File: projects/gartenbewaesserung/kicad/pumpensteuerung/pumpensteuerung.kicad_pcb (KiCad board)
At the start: 2 copper layers, 100 x 85 mm, 26 parts, among them J1 Screw_Terminal_01x03, J2 Screw_Terminal_01x02, J3 I2C Terminal, J4 Screw_Terminal_01x03, J5 Screw_Terminal_01x03, K2 SANYOU_SRD_Form_C, K3 SANYOU_SRD_Form_C, K4 SANYOU_SRD_Form_C, Q1 S8050, Q2 S8050, Q3 S8050

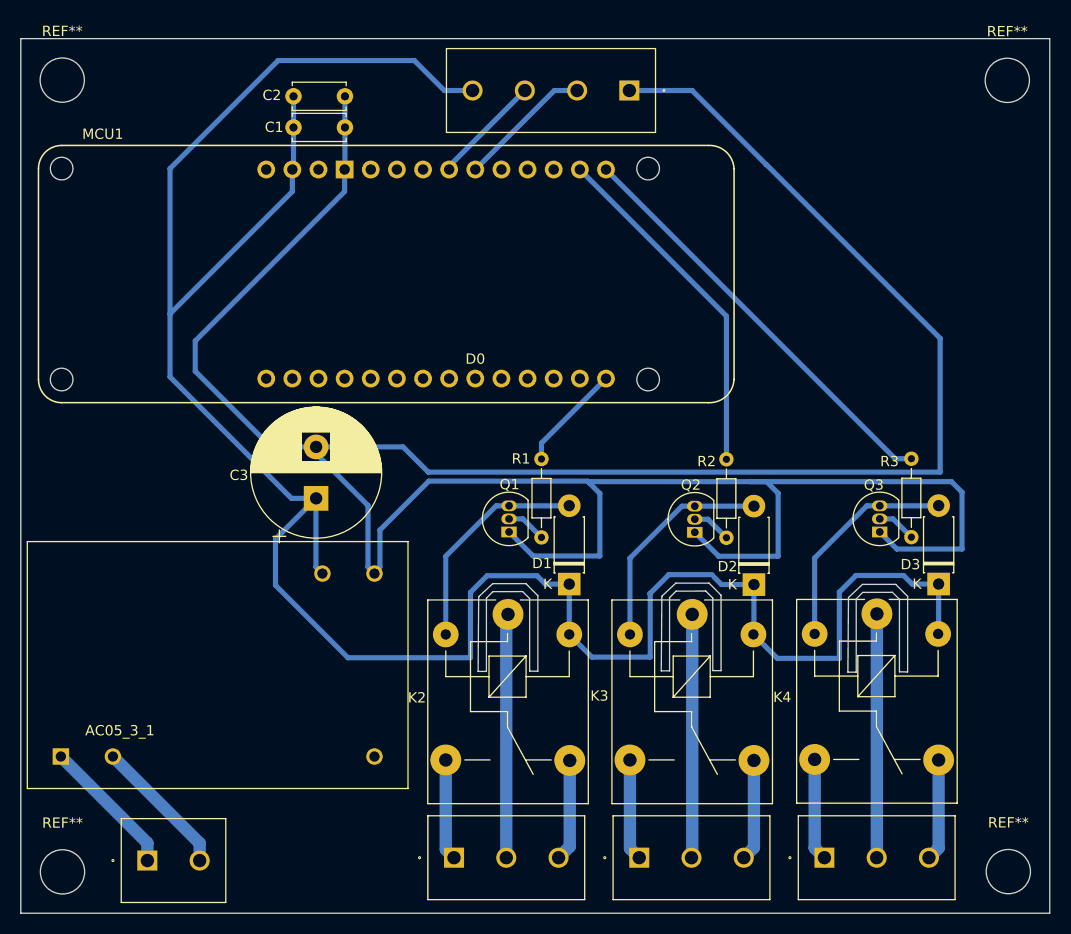
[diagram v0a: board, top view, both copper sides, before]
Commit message: [gartenbewaesserung(pcb)] change resistor to 220 Ohm
1k was a little bit too much, for 3.3V.
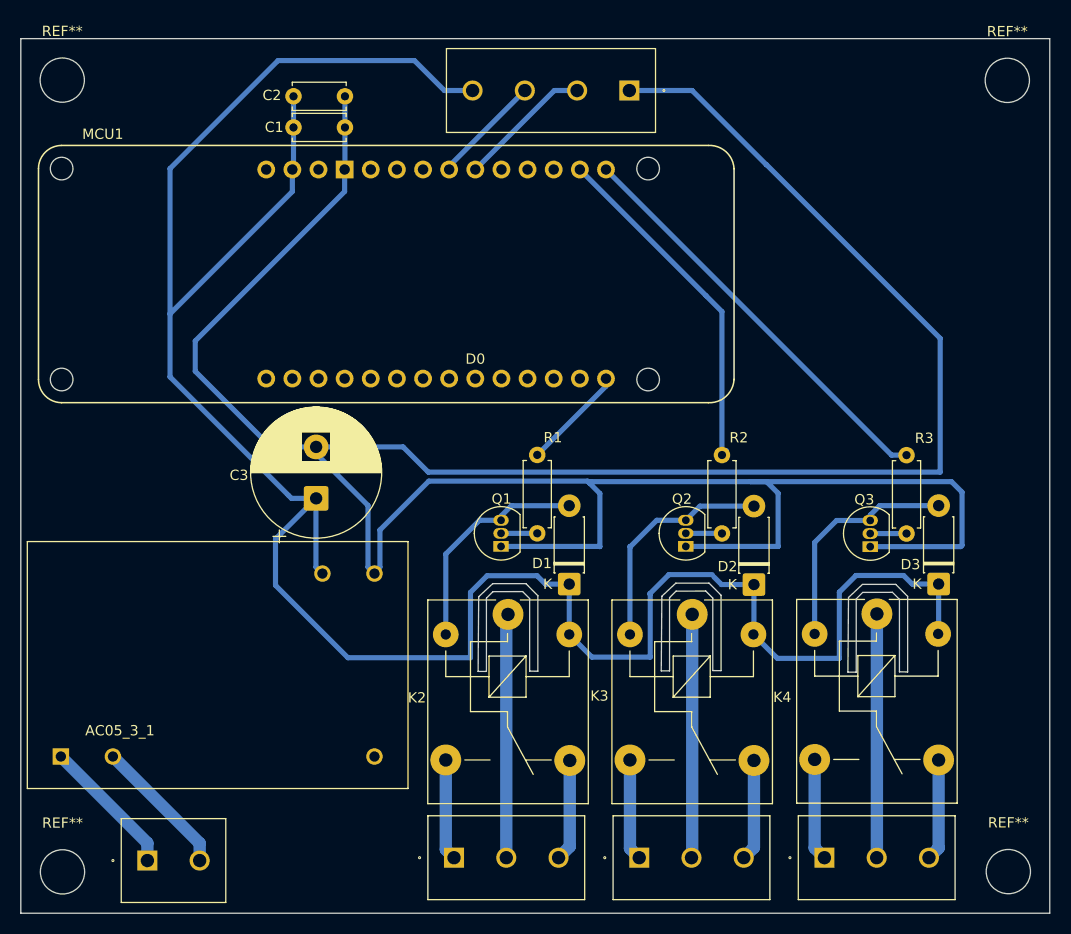
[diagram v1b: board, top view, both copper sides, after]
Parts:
- R1, R2, R3: value 1k -> 220; footprint Resistor_THT:R_Axial_DIN0204_L3.6mm_D1.6mm_P7.62mm_Horizontal -> Resistor_THT:R_Axial_DIN0207_L6.3mm_D2.5mm_P7.62mm_Horizontal
- moved Q3 1.70 mm to (133.1, 98.4)
- moved Q2 1.62 mm to (115.1, 98.3)
- moved Q1 1.61 mm to (97.2, 98.3)
- moved R2 0.60 mm to (118.6, 89.5)
- moved R3 0.59 mm to (136.6, 89.5)
- moved R1 0.57 mm to (100.7, 89.5)
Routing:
- net /-5V: track 292.4 -> 290.2 mm
- net Net-(D3-A): track 21.5 -> 22.8 mm
- net Net-(D2-A): track 21.6 -> 22.2 mm
- net /Poolrelais: track 41.3 -> 40.7 mm

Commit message: [gartenbewasserung(pcb)] replace Q8050 with a 2N3904
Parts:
- Q1, Q2, Q3: value S8050 -> 2N3904
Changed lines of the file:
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@@
 			)
 		)
-		(property "Value" "S8050"
+		(property "Value" "2N3904"
 			(at -2.26 -0.275 180)
 			(layer "F.Fab")
@@
 			)
 		)
-		(property "Datasheet" "http://www.unisonic.com.tw/datasheet/S8050.pdf"
+		(property "Datasheet" "https://www.onsemi.com/pub/Collateral/2N3903-D.PDF"
 			(at 0 0 90)
 			(unlocked yes)
@@
 			)
 		)
-		(property "Description" "0.7A Ic, 20V Vce, Low Voltage High Current NPN Transistor, TO-92"
+		(property "Description" "0.2A Ic, 40V Vce, Small Signal NPN Transistor, TO-92"
 			(at 0 0 90)
 			(unlocked yes)
@@
 			)
 		)
-		(property "Value" "S8050"
+		(property "Value" "2N3904"
 			(at -2.18 -0.175 180)
 			(layer "F.Fab")
@@
 			)
 		)
-		(property "Datasheet" "http://www.unisonic.com.tw/datasheet/S8050.pdf"
+		(property "Datasheet" "https://www.onsemi.com/pub/Collateral/2N3903-D.PDF"
 			(at 0 0 90)
 			(unlocked yes)
@@
 			)
 		)
-		(property "Description" "0.7A Ic, 20V Vce, Low Voltage High Current NPN Transistor, TO-92"
+		(property "Description" "0.2A Ic, 40V Vce, Small Signal NPN Transistor, TO-92"
 			(at 0 0 90)
 			(unlocked yes)
@@
 			)
 		)
-		(property "Value" "S8050"
+		(property "Value" "2N3904"
 			(at -2.253 -0.124 180)
 			(layer "F.Fab")
@@
 			)
 		)
-		(property "Datasheet" "http://www.unisonic.com.tw/datasheet/S8050.pdf"
+		(property "Datasheet" "https://www.onsemi.com/pub/Collateral/2N3903-D.PDF"
 			(at 0 0 90)
 			(unlocked yes)
@@
 			)
 		)
-		(property "Description" "0.7A Ic, 20V Vce, Low Voltage High Current NPN Transistor, TO-92"
+		(property "Description" "0.2A Ic, 40V Vce, Small Signal NPN Transistor, TO-92"
 			(at 0 0 90)
 			(unlocked yes)

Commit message: [gartenbewaesserung(pcb)] add MPN to easier pcb ordering
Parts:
- C1: value 10 nF -> 10000pF 100V 10% Y5P 5mm
- C2: value 100 nF -> 0.1uF 500V +80/-20%
- C3: value 1000 µF -> 1000 µF, 25 V, 105°C, low ESR, 12,5 x 20 mm, RM 5
- R1, R2, R3: value 220 -> 220 Ohm, axial, 250 mW, 0,1%

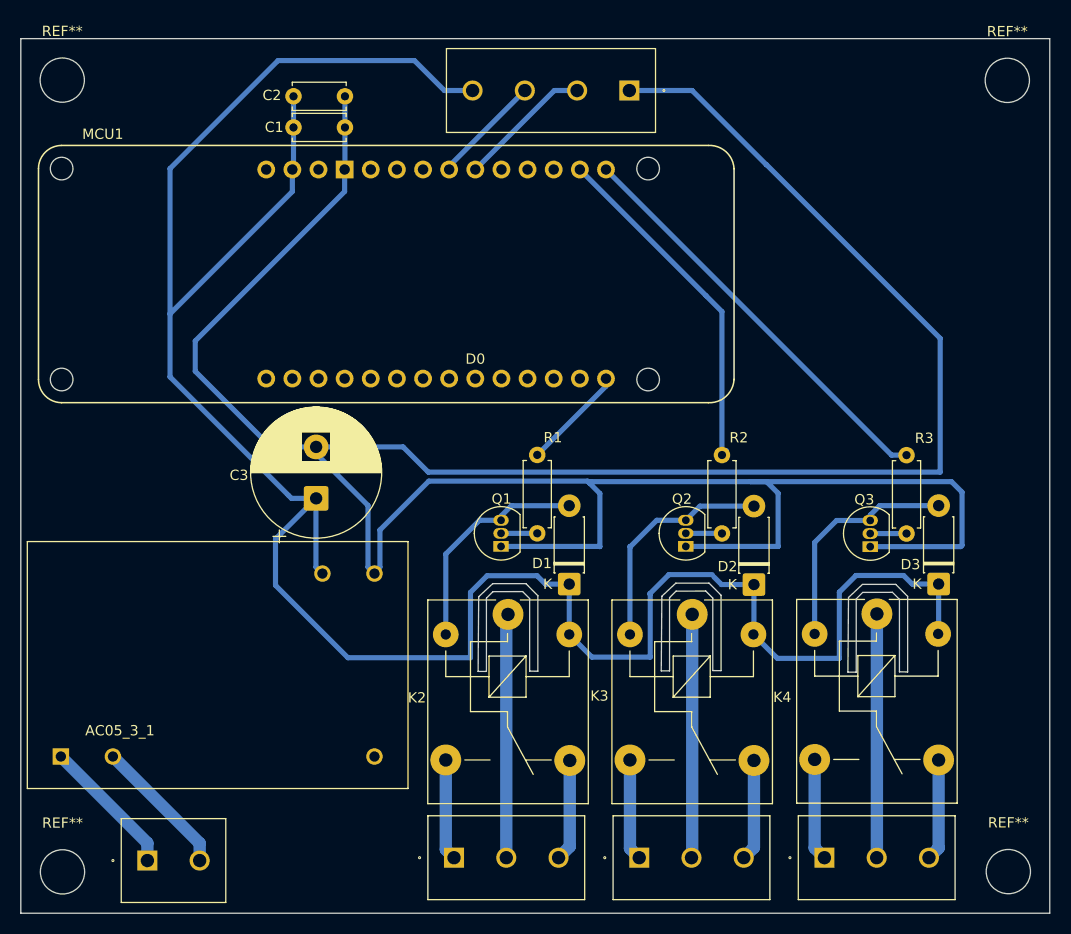
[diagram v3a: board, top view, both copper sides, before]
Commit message: [gartenbewaesserung(pcb)] remove screw terminal for i2c
currently we do not need it. and we will never do, we will use modbus
(rs485) to switch relais.

the relais module will be created later. and if we know that is the way
to go we will add rs485 functionality also to the pump.
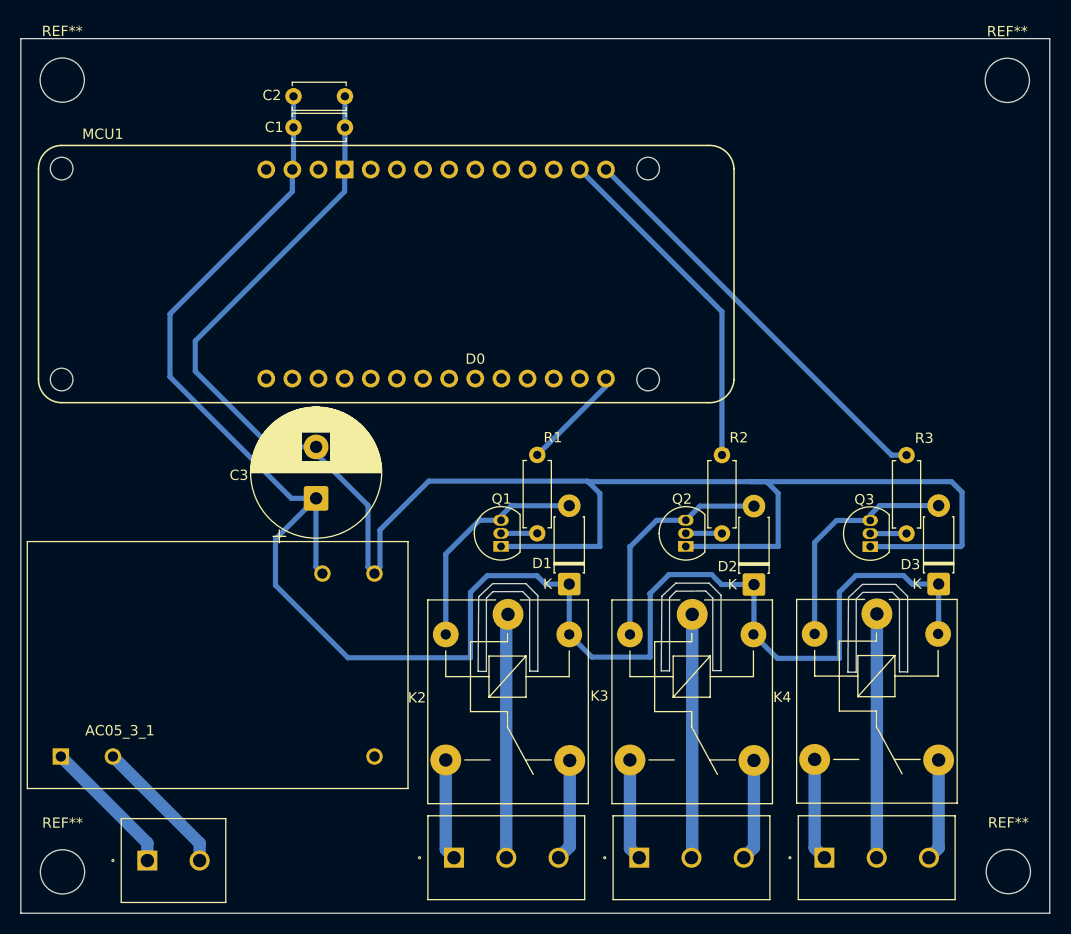
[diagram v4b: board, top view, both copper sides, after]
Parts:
- removed J3: I2C Terminal, PhoenixContact:MKDSN 1,5_4-5,08
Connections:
- MCU1 pad D11: /SDA -> unconnected-(MCU1-D11/SDA-PadD11)
- MCU1 pad D12: /SCL -> unconnected-(MCU1-D12/SCL-PadD12)
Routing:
- net /-5V: track 290.2 -> 175.4 mm
- net /+5V: track 226.3 -> 177.2 mm
- net /SDA: track 13.2 -> 0.00 mm
- net /SCL: track 10.7 -> 0.00 mm

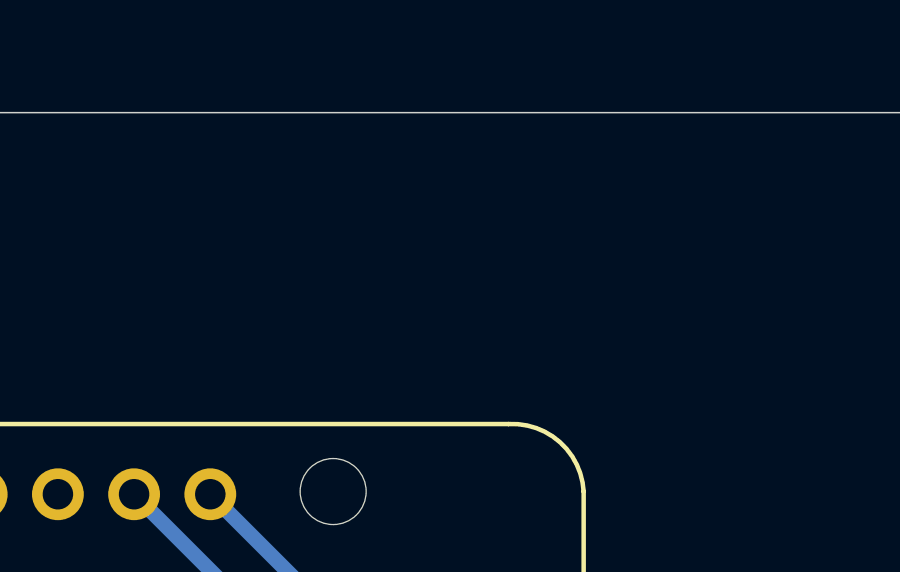
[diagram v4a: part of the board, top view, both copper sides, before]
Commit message: [gartenbewaesserung(pcb)] add oshw logo
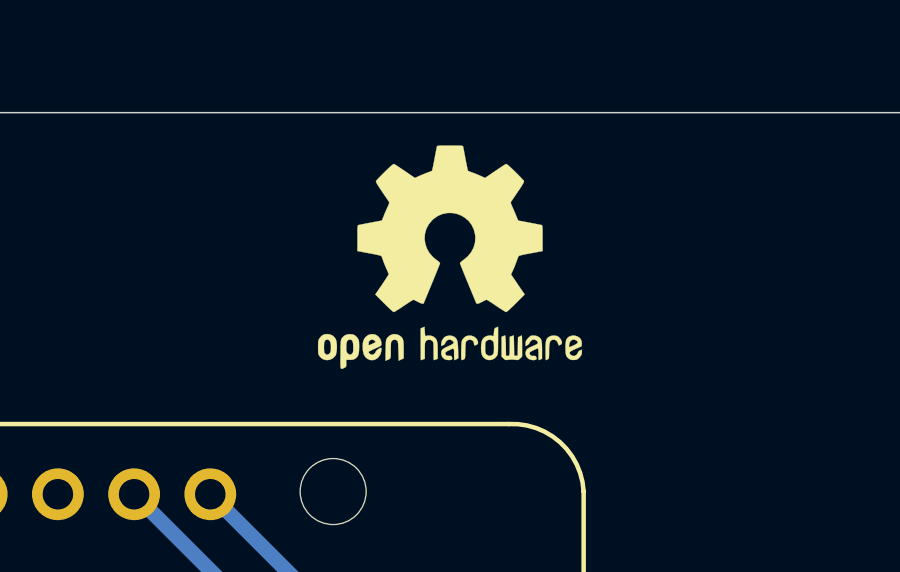
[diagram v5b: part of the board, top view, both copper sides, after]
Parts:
- added REF**: OSHW-Logo2_9.8x8mm_SilkScreen, Symbol:OSHW-Logo2_9.8x8mm_SilkScreen, F.Cu at (115.4, 53.8)

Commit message: [gartenbewaesserung(pcb)] replace resistor with one from vishay
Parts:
- R1, R2, R3: value 220 Ohm, axial, 250 mW, 0,1% -> 220 OHM 0.6W 1% AXIAL
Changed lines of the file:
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@@
 			)
 		)
-		(property "Value" "220 Ohm, axial, 250 mW, 0,1%"
+		(property "Value" "220 OHM 0.6W 1% AXIAL"
 			(at 3.81 2.37 270)
 			(layer "F.Fab")
@@
 			)
 		)
-		(property "Datasheet" ""
+		(property "Datasheet" "https://www.vishay.com/docs/28766/mbxsma.pdf"
 			(at 0 0 270)
 			(layer "F.Fab")
@@
 			)
 		)
-		(property "MPN" " RC55Y-220RBI"
+		(property "MPN" "MBB02070C2200FCT00"
 			(at 0 0 270)
 			(unlocked yes)
@@
 			)
 		)
-		(property "Value" "220 Ohm, axial, 250 mW, 0,1%"
+		(property "Value" "220 OHM 0.6W 1% AXIAL"
 			(at 3.81 2.37 270)
 			(layer "F.Fab")
@@
 			)
 		)
-		(property "Datasheet" ""
+		(property "Datasheet" "https://www.vishay.com/docs/28766/mbxsma.pdf"
 			(at 0 0 270)
 			(layer "F.Fab")
@@
 			)
 		)
-		(property "MPN" " RC55Y-220RBI"
+		(property "MPN" "MBB02070C2200FCT00"
 			(at 0 0 270)
 			(unlocked yes)
@@
 			)
 		)
-		(property "Value" "220 Ohm, axial, 250 mW, 0,1%"
+		(property "Value" "220 OHM 0.6W 1% AXIAL"
 			(at 3.81 2.37 270)
 			(layer "F.Fab")
@@
 			)
 		)
-		(property "Datasheet" ""
+		(property "Datasheet" "https://www.vishay.com/docs/28766/mbxsma.pdf"
 			(at 0 0 270)
 			(layer "F.Fab")
@@
 			)
 		)
-		(property "MPN" " RC55Y-220RBI"
+		(property "MPN" "MBB02070C2200FCT00"
 			(at 0 0 270)
 			(unlocked yes)
